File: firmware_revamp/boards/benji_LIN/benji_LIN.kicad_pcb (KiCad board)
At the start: 2 copper layers, 42.9 x 81 mm, 37 parts, among them J1 CONN_02X03, J2 Conn_01x11, J3 Conn_01x11, J4 CONN_01X03, J5 CONN_01x02, J6 CONN_01X03, J7 CONN_01x02, U1 MCP2561-E_SN, U2 ATMEGA16M1, U3 TLIN1021DRQ1, Y1 Crystal_SMD

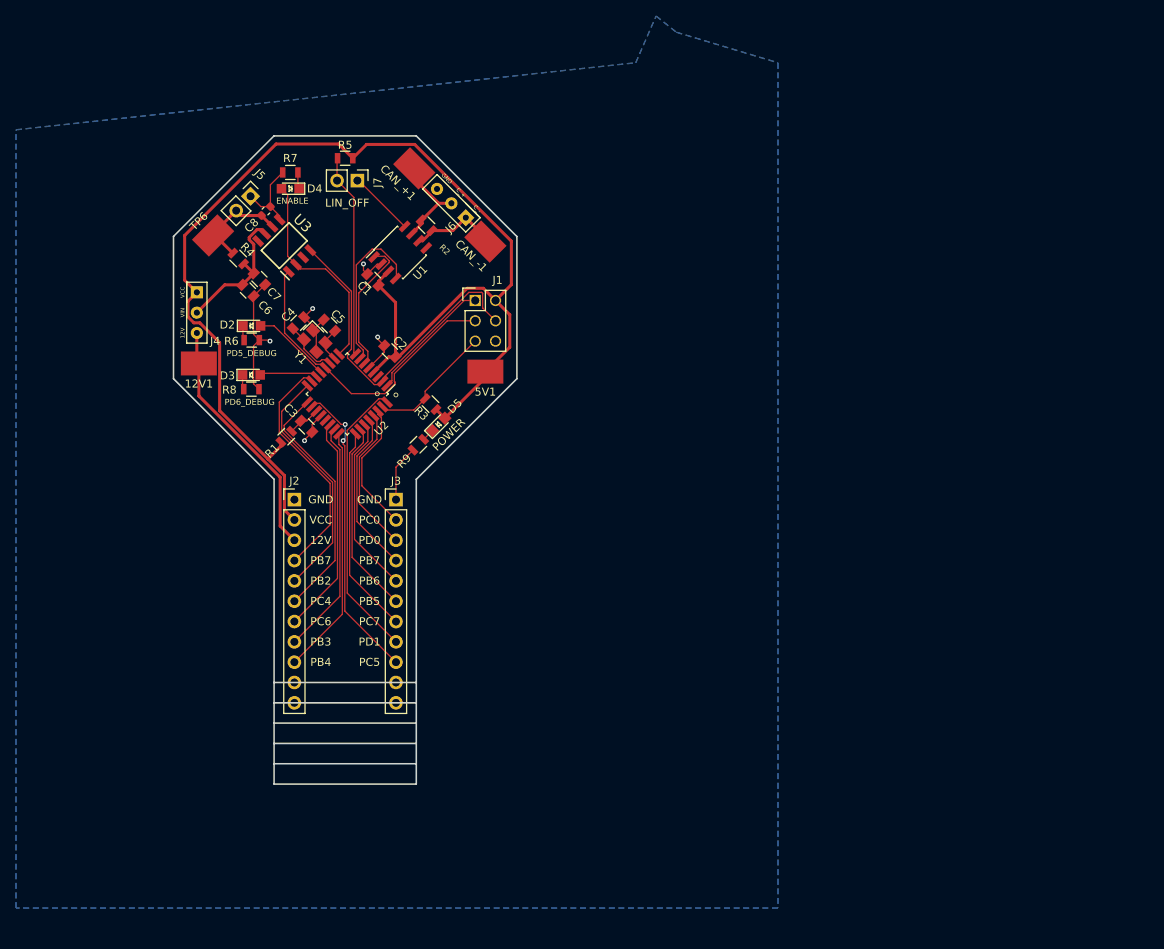
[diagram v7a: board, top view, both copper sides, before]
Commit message: Used correct headers, renamed pins where necessary
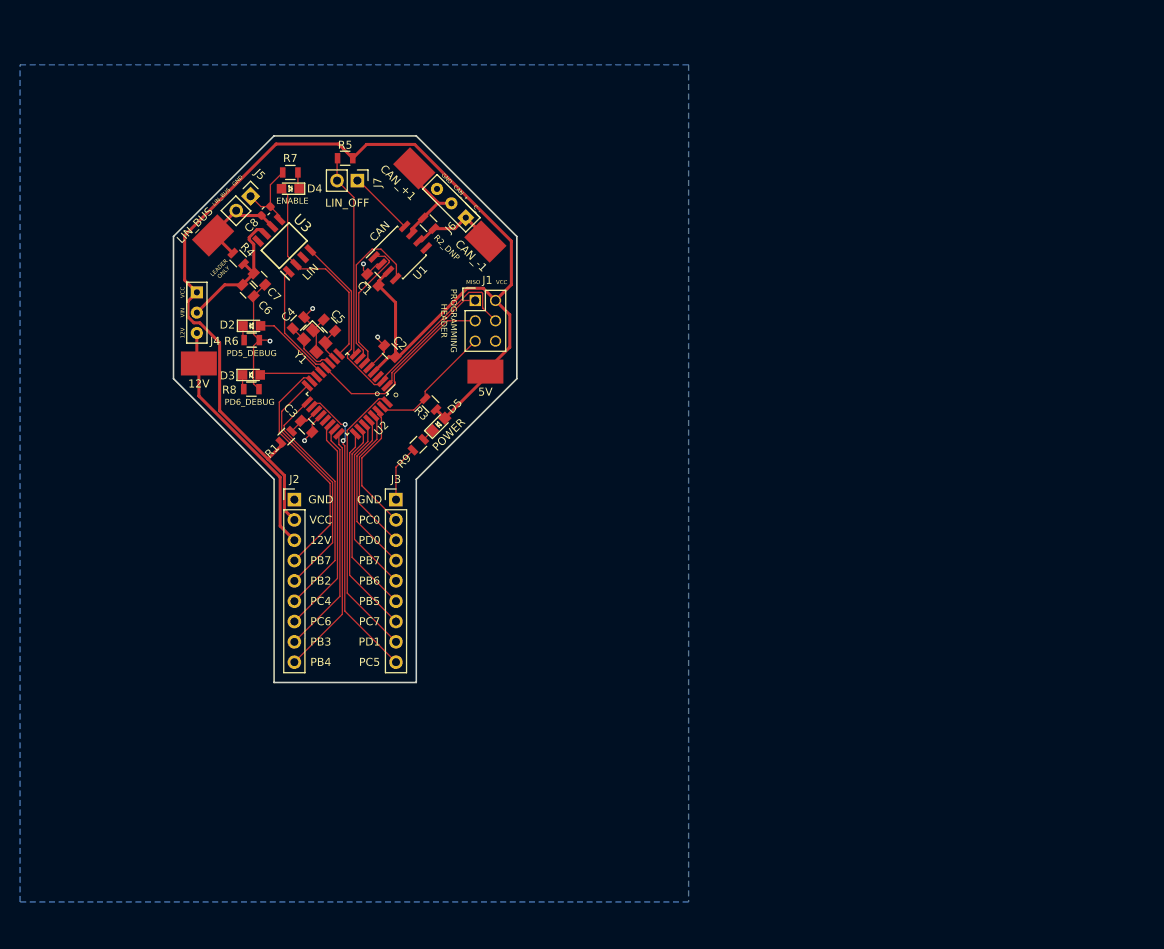
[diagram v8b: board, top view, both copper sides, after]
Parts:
- J2, J3: value Conn_01x11 -> Conn_01x09; footprint footprints:PinHeader_1x11_P2.54mm_Vertical -> footprints:PinHeader_1x9_P2.54mm_Vertical
- moved R2_DNP 0.36 mm to (118.6, 65.8)
- renumbered 12V1 to 12V, 5V1 to 5V, TP6 to LIN_BUS, R2 to R2_DNP
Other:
- board size 42.9 x 81 mm -> 42.9 x 68.3 mm
- board text added: "CAN"
- board text added: "CAN_+"
- board text added: "LEADER ONLY"
- board text added: "LIN"
- board text added: "LIN_BUS"
- board text added: "MISO"
- board text added: "PROGRAMMING HEADER"
- board text removed: "C_+"
